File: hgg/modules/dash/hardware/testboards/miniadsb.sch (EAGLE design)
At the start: 17 parts, among them IC1 TLC272P, IC2 LM339N, IC3 7414N

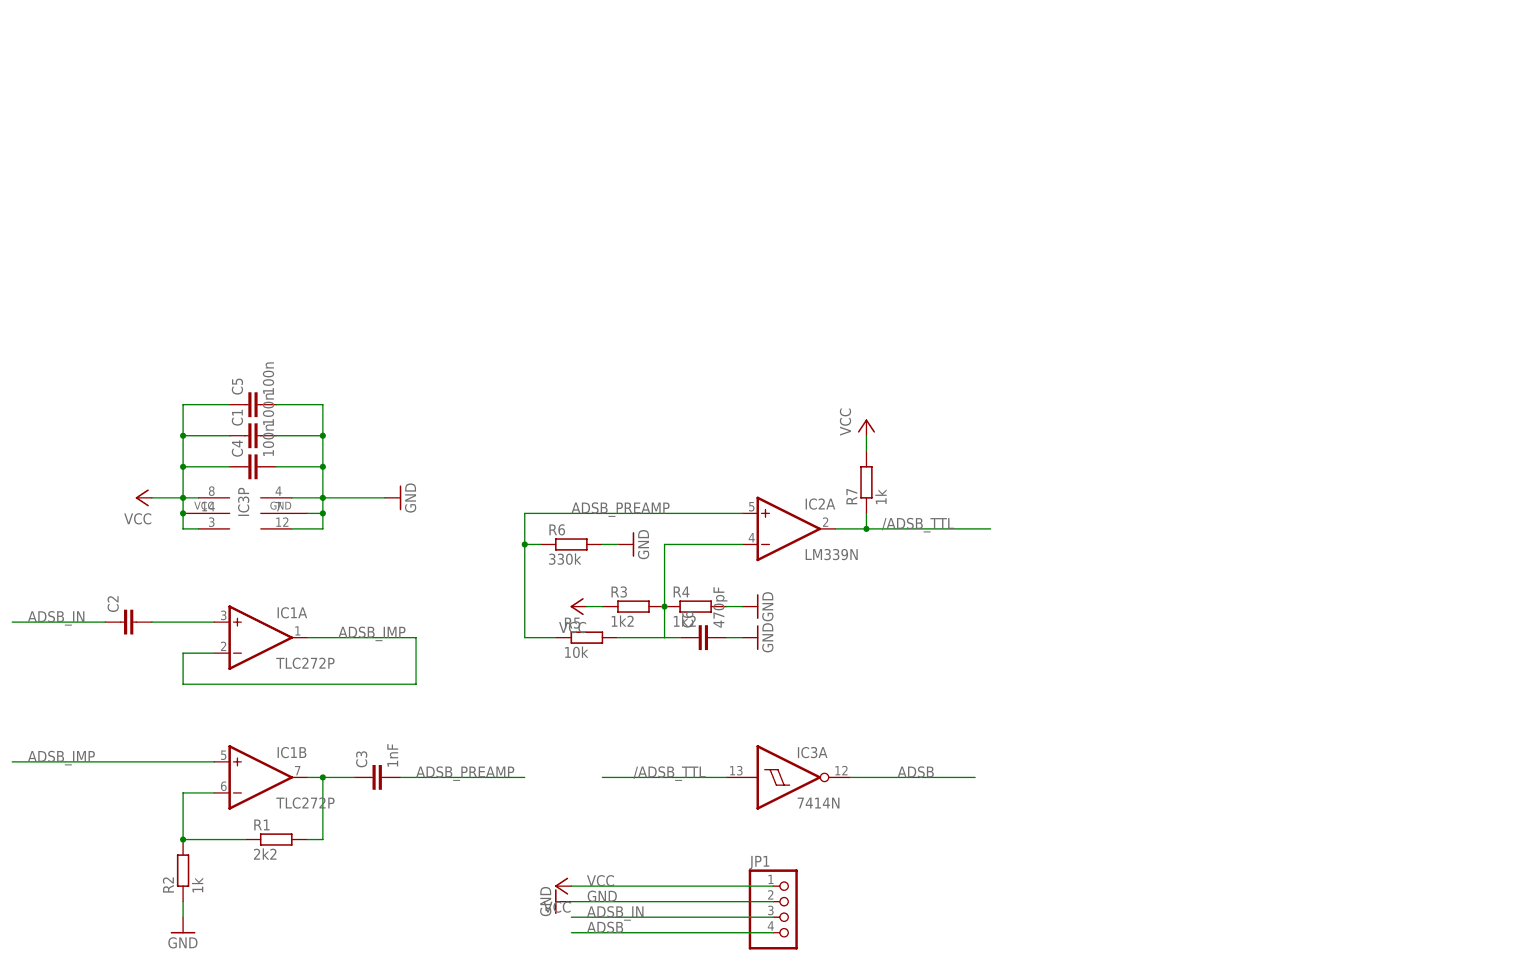
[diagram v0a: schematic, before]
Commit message: reduced component count, TLC: replaced TRT with SMD variant, layout redone
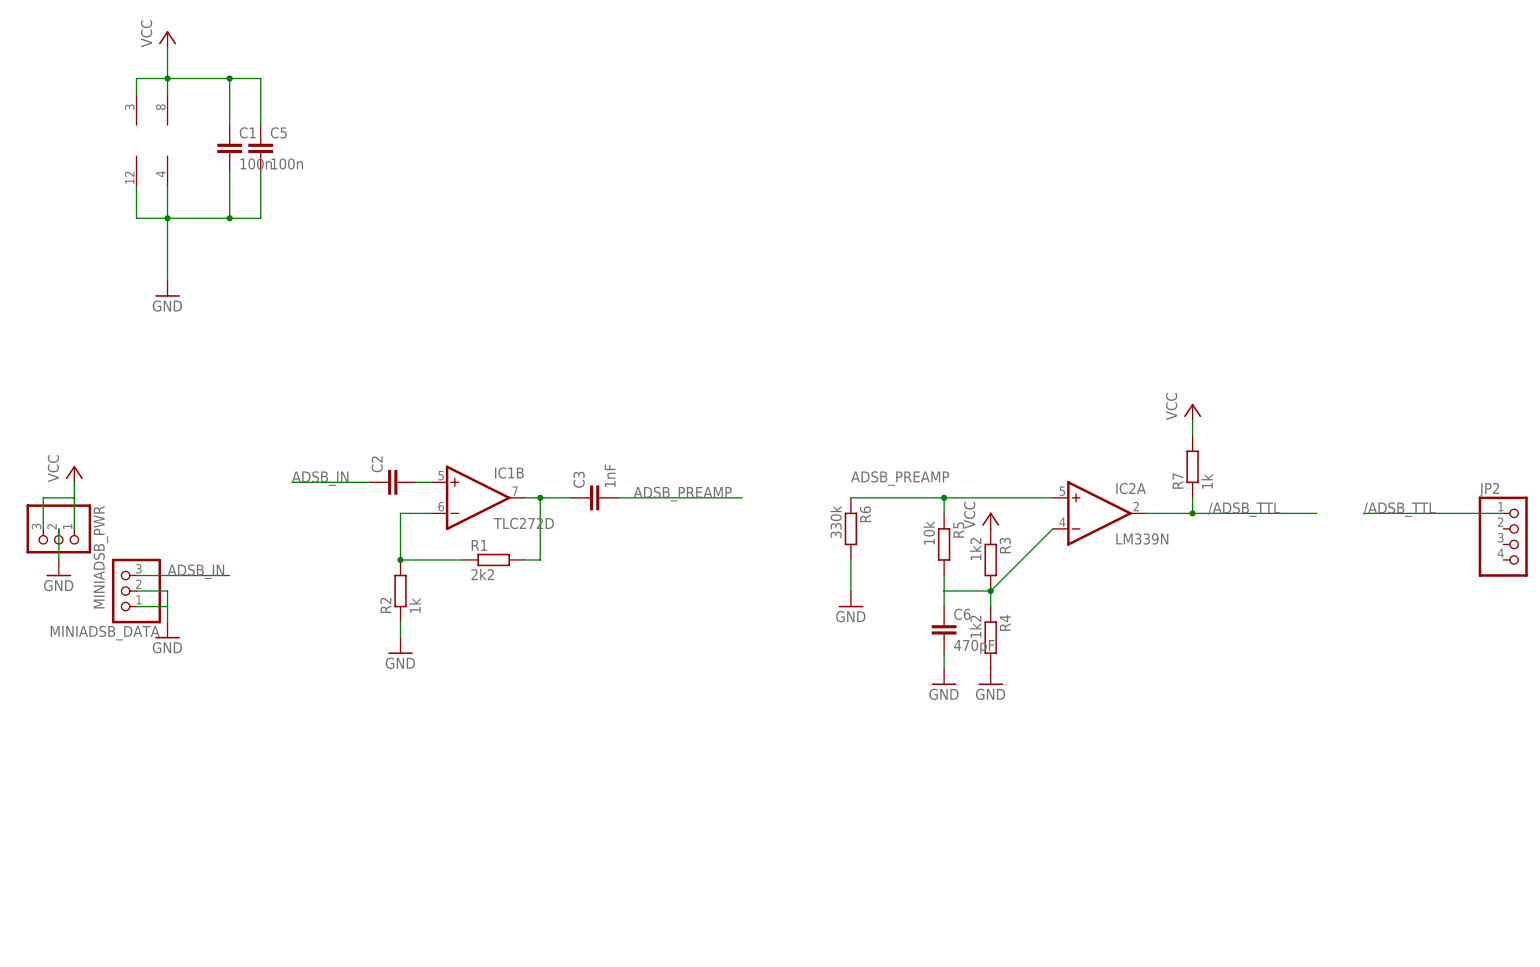
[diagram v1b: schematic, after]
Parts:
- removed C4: 100n, resistor:C-EUC0805
- removed IC3: 7414N, 74xx-us:7414N
- removed JP1: (no value), pinhead:PINHD-1X4
- added JP2: (no value), pinhead:PINHD-1X4
- added MINIADSB_DATA, MINIADSB_PWR: (no value), pinhead:PINHD-1X3
- IC1: value TLC272P -> TLC272D; device linear:TLC272P -> linear:TLC272D
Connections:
- removed net ADSB: IC3A.O, JP1.4
- removed net ADSB_IMP: IC1A.-IN, IC1A.OUT, IC1B.+IN
- net /ADSB_TTL: now also JP2.1; no longer IC3A.I
- net ADSB_IN: now also MINIADSB_DATA.3; no longer JP1.3
- net GND: now also MINIADSB_DATA.1, MINIADSB_DATA.2, MINIADSB_PWR.2; no longer C4.2, IC3P.GND, JP1.2
- net N$1: now also IC1B.+IN; no longer IC1A.+IN
- net VCC: now also MINIADSB_PWR.1, MINIADSB_PWR.3; no longer C4.1, IC3P.VCC, JP1.1
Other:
- moved on the sheet: C1, C2, C3, C5, C6, IC1B, IC2A, R1, R2, R3, R4, R5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
